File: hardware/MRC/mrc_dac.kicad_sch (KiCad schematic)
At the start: 75 parts, among them U1 DAC5687IPZP

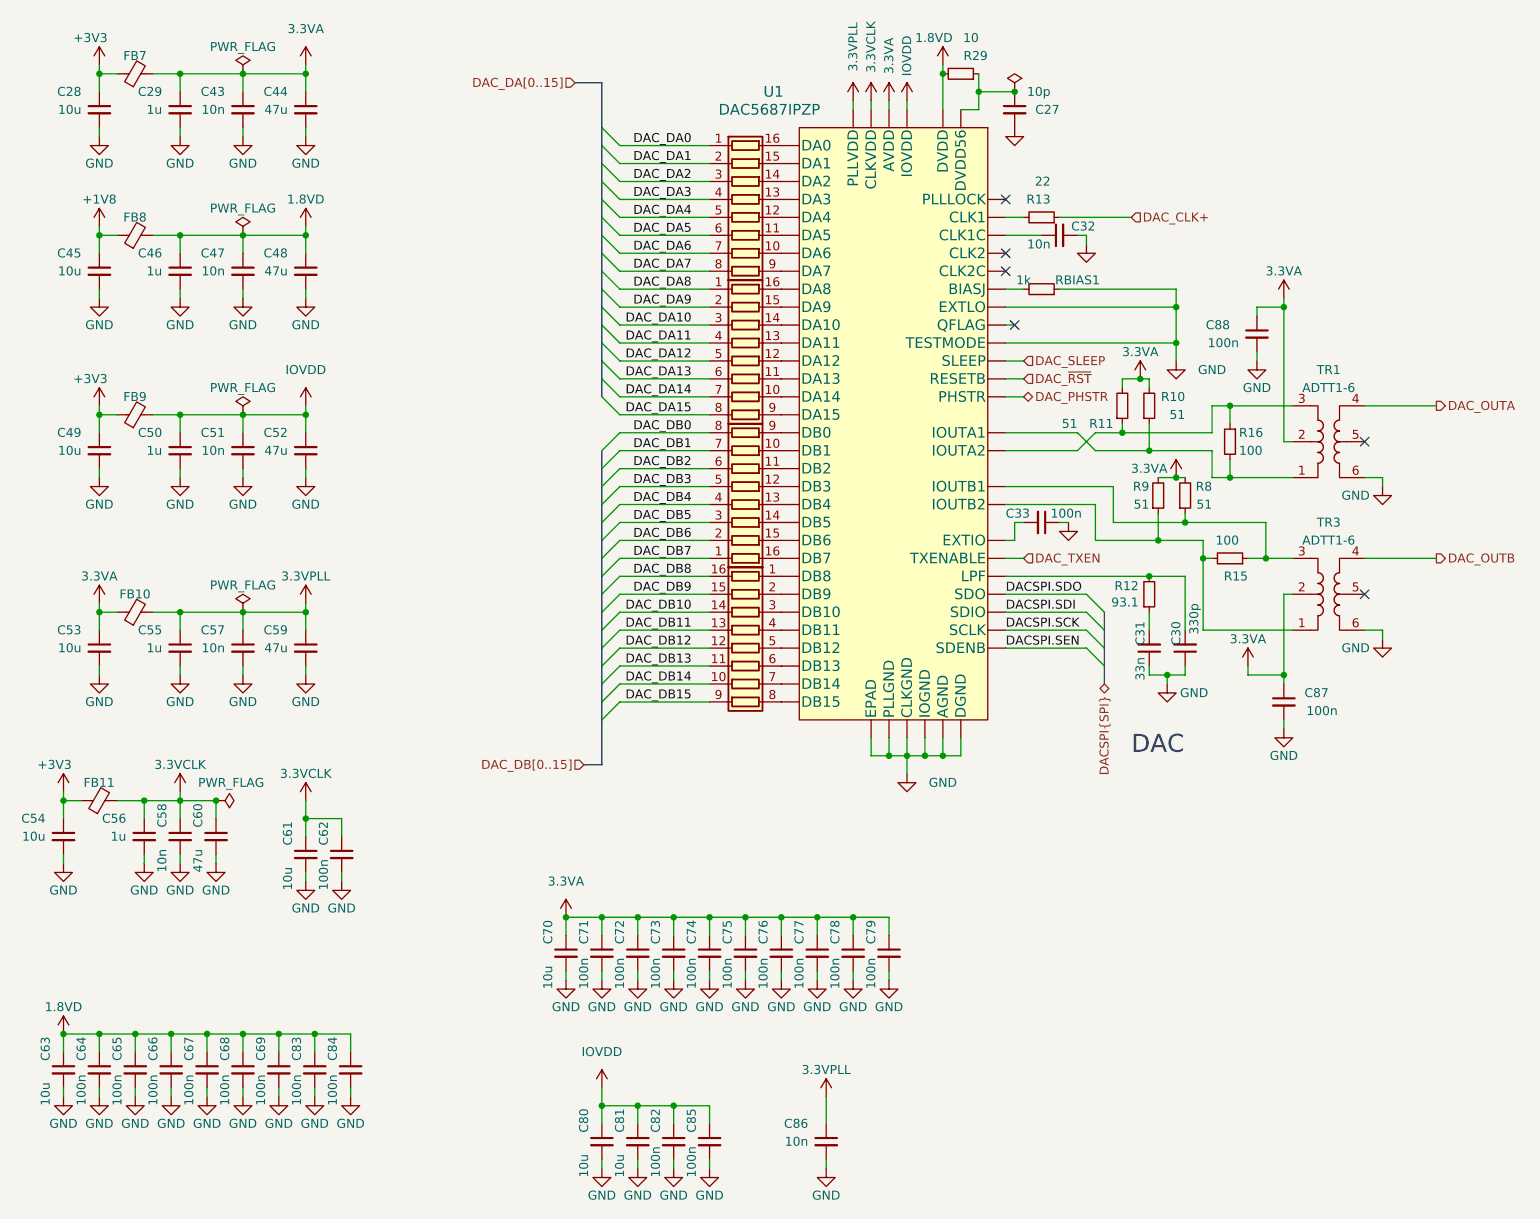
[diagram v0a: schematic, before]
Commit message: Update KiCAD Version, Integrate Libraries
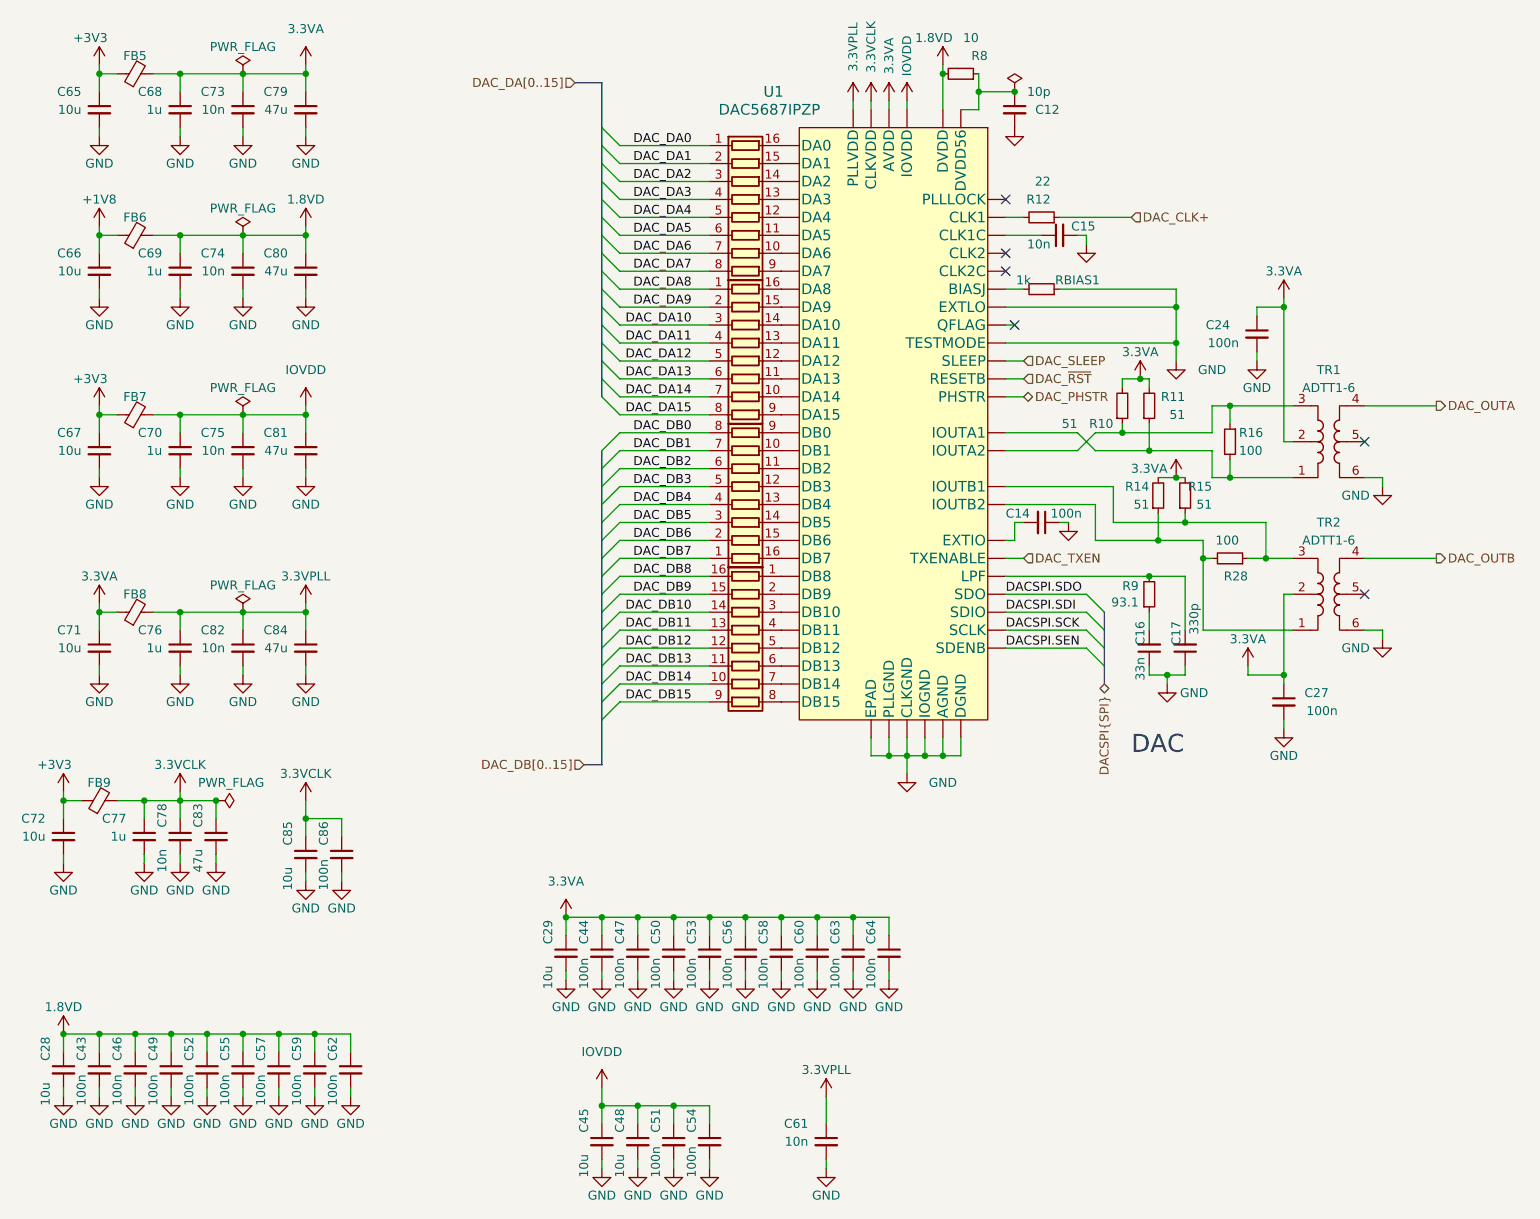
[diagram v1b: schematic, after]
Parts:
- renumbered C27 to C12, C33 to C14, C32 to C15, C31 to C16, C30 to C17, C88 to C24, C87 to C27, C63 to C28, C70 to C29, C64 to C43, C71 to C44, C80 to C45, C65 to C46, C72 to C47, C81 to C48, C66 to C49, C73 to C50, C82 to C51, C67 to C52, C74 to C53, C85 to C54, C68 to C55, C75 to C56, C69 to C57, C76 to C58, C83 to C59, C77 to C60, C86 to C61, C84 to C62, C78 to C63, C79 to C64, C28 to C65, C45 to C66, C49 to C67, C29 to C68, C46 to C69, C50 to C70, C53 to C71, C54 to C72, C43 to C73, C47 to C74, C51 to C75, C55 to C76, C56 to C77, C58 to C78, C44 to C79, C48 to C80, C52 to C81, C57 to C82, C60 to C83, C59 to C84, C61 to C85, C62 to C86, FB7 to FB5, FB8 to FB6, FB9 to FB7, FB10 to FB8, FB11 to FB9, R11 to R10, R10 to R11, R13 to R12, R9 to R14, R8 to R15, R15 to R28, R29 to R8, R12 to R9, RN6 to RN3, RN3 to RN4, RN4 to RN5, RN5 to RN6, TR3 to TR2

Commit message: Clean bill of materials
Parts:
- C12: MPN (none) -> KGM15ACG2A100FT
- C14, C24, C27, C43, C44, C46, C47, C49, C50, C51, C52, C53, C54, C55, C56, C57, C58, C59, C60, C62, C63, C64, C86: MPN (none) -> C0603C104K1RACAUTO
- C15, C61, C73, C74, C75, C78, C82: MPN (none) -> KAM15AR72A103KT
- C16: MPN (none) -> KGM15BR71E333KT
- C17: MPN (none) -> KGM15AR71E331KT
- C28, C29, C45, C48, C65, C66, C67, C71, C72, C85: MPN (none) -> KGM15CR51A106MT
- C68, C69, C70, C76, C77: MPN (none) -> KGM15BR51E105KM
- C79, C80, C81, C83, C84: MPN (none) -> KGM15CR50J476MT
- FB5, FB6, FB7, FB8, FB9: MPN (none) -> 742792641
- R10, R11, R14, R15: MPN (none) -> SDR03EZPF51R0
- R12: MPN (none) -> ESR03EZPJ220
- R16, R28: MPN (none) -> SDR03EZPD1000
- R8: MPN (none) -> CMP0603AFX-10R0L
- R9: MPN (none) -> CRCW0603-93.1-E3
- RBIAS1: MPN (none) -> CRCW06031K00DHEBP
- U1: MPN (none) -> DAC5687IPZP
